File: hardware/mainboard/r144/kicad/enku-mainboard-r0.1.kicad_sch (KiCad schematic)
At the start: 0 parts

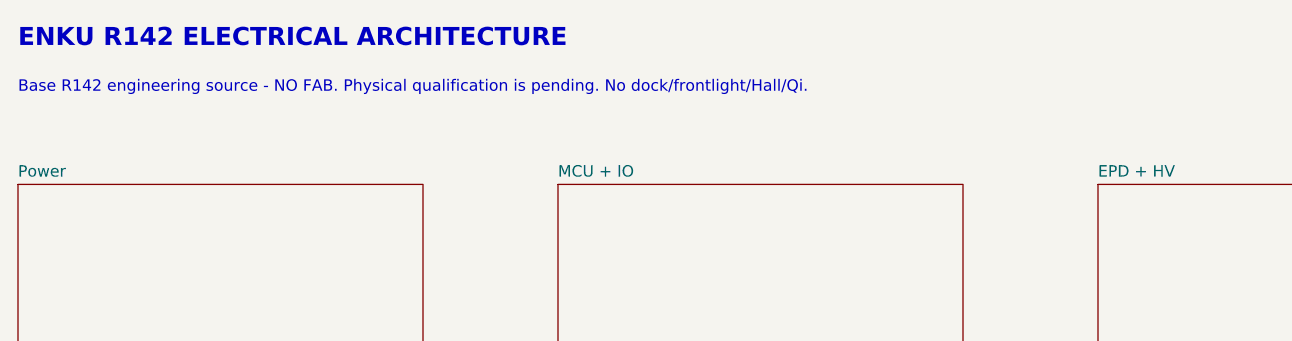
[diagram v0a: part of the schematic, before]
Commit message: R144: synchronize schematic titles and confirmed panel annotation; correct informational divider current
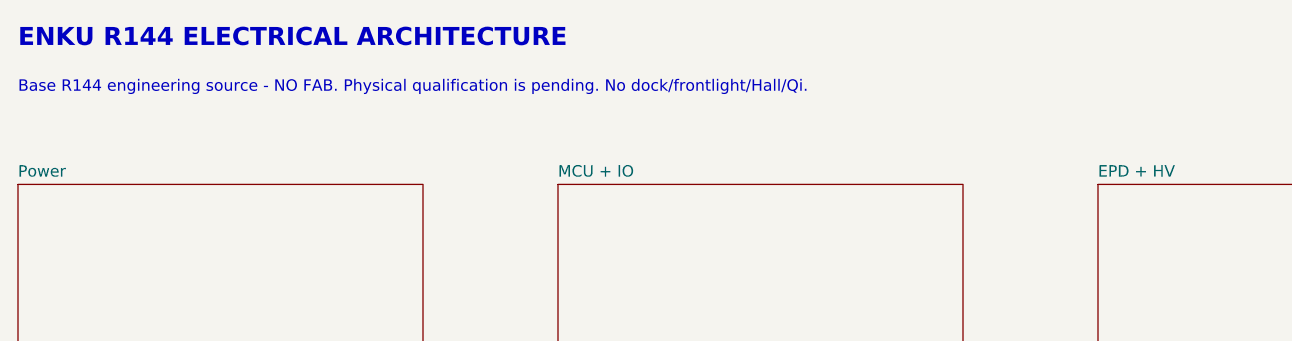
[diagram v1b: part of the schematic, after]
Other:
- note added: "Base R144 engineering source - NO FAB. Physical qualification is pending. No dock/frontlight/Hall/Qi."
- note added: "ENKU R144 ELECTRICAL ARCHITECTURE"
- note removed: "Base R142 engineering source - NO FAB. Physical qualification is pending. No dock/frontlight/Hall/Qi."
- note removed: "ENKU R142 ELECTRICAL ARCHITECTURE"
- title: ENKU Mainboard R142 -> ENKU Mainboard R144
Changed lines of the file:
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@@
 	(paper "A4")
 	(title_block
-		(title "ENKU Mainboard R142")
-		(date "2026-10-14")
+		(title "ENKU Mainboard R144")
+		(date "2026-10-15")
 		(rev "R144 - ENGINEERING / NO FAB")
 		(company "ENKU open-source e-reader")
 		(comment 1 "Hierarchical schematic capture baseline")
-		(comment 2 "NOT FABRICATION READY until ERC + exact footprint review")
+		(comment 2 "NO FAB - physical parts and process qualification pending")
 	)
 	(sheet (at 25 35) (size 45 28) (fields_autoplaced)
@@
 		)
 	)
-	(text "ENKU R142 ELECTRICAL ARCHITECTURE" (exclude_from_sim no) (at 25 20 0)
+	(text "ENKU R144 ELECTRICAL ARCHITECTURE" (exclude_from_sim no) (at 25 20 0)
 		(effects (font (size 2 2) (bold yes)) (justify left bottom))
 	)
-	(text "Base R142 engineering source - NO FAB. Physical qualification is pending. No dock/frontlight/Hall/Qi." (exclude_from_sim no) (at 25 25 0)
+	(text "Base R144 engineering source - NO FAB. Physical qualification is pending. No dock/frontlight/Hall/Qi." (exclude_from_sim no) (at 25 25 0)
 		(effects (font (size 1.27 1.27)) (justify left bottom))
 	)
